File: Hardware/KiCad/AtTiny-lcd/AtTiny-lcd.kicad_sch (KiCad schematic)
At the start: 7 parts, among them J1 Conn_01x04_Pin, J2 Conn_01x04_Pin, Q1 BC817, U1 ATtiny414-SS

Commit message: cleanup #1
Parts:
- added C1: 100n, symbol Device:C
- R1: value R -> 1k
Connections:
- net +5V: now also C1.1
- net GND: now also C1.2
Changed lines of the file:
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@@
+	)
+	(junction
+		(at 81.28 116.84)
+		(diameter 0)
+		(color 0 0 0 0)
 	)
 	(junction
@@
 	)
 	(junction
+		(at 81.28 127)
+		(diameter 0)
+		(color 0 0 0 0)
+	)
+	(junction
 		(at 72.39 109.22)
 		(diameter 0)
@@
 	(wire
 		(pts
+			(xy 81.28 116.84) (xy 81.28 118.11)
+		)
+		(stroke
+			(width 0)
+			(type default)
+		)
+	)
+	(wire
+		(pts
 			(xy 88.9 121.92) (xy 88.9 95.25)
 		)
@@
 	(wire
 		(pts
+			(xy 81.28 125.73) (xy 81.28 127)
+		)
+		(stroke
+			(width 0)
+			(type default)
+		)
+	)
+	(wire
+		(pts
 			(xy 107.95 115.57) (xy 107.95 127)
 		)
@@
 	(wire
 		(pts
-			(xy 104.14 127) (xy 72.39 127)
+			(xy 104.14 127) (xy 81.28 127)
 		)
 		(stroke
@@
 		(pts
 			(xy 196.85 81.28) (xy 187.96 81.28)
+		)
+		(stroke
+			(width 0)
+			(type default)
+		)
+	)
+	(wire
+		(pts
+			(xy 81.28 127) (xy 72.39 127)
 		)
 		(stroke
@@
 			)
 		)
-		(property "Value" "R"
+		(property "Value" "1k"
 			(at 184.15 118.11 90)
 			(effects
@@
 					(unit 1)
 				)
+			)
+		)
+	)
+	(symbol
+		(lib_id "Device:C")
+		(at 81.28 121.92 0)
+		(unit 1)
+		(exclude_from_sim no)
+		(in_bom yes)
+		(on_board yes)
+		(dnp no)
+		(fields_autoplaced yes)
+		(property "Reference" "C1"
+			(at 85.09 120.6499 0)
+			(effects
+				(font
+					(size 1.27 1.27)
+				)
+				(justify left)
+			)
+		)
+		(property "Value" "100n"
+			(at 85.09 123.1899 0)
+			(effects
+				(font
+					(size 1.27 1.27)
+				)
+				(justify left)
+			)
+		)
+		(property "Footprint" ""
+			(at 82.2452 125.73 0)
+			(effects
+				(font
+					(size 1.27 1.27)
+				)
+				(hide yes)
+			)
+		)
+		(property "Datasheet" "~"
+			(at 81.28 121.92 0)
+			(effects
+				(font
+					(size 1.27 1.27)
+				)
+				(hide yes)
+			)
+		)
+		(property "Description" "Unpolarized capacitor"
+			(at 81.28 121.92 0)
+			(effects
+				(font
+					(size 1.27 1.27)
+				)
+				(hide yes)
+			)
+		)
+		(pin "2"
+		)
+		(pin "1"
+		)
+		(instances
+			(project "AtTiny-lcd"
+				(path "/788c3613-b442-483a-8dfb-af18bcc54a06"
+					(reference "C1")
+					(unit 1)
+				)

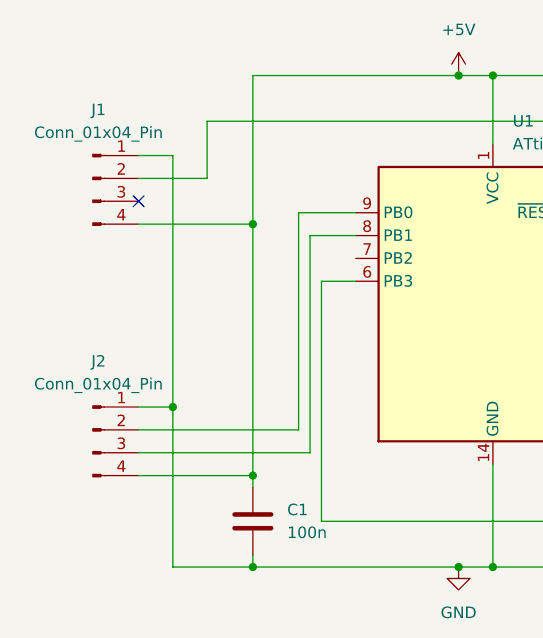
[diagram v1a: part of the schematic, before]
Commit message: Backlight dimming
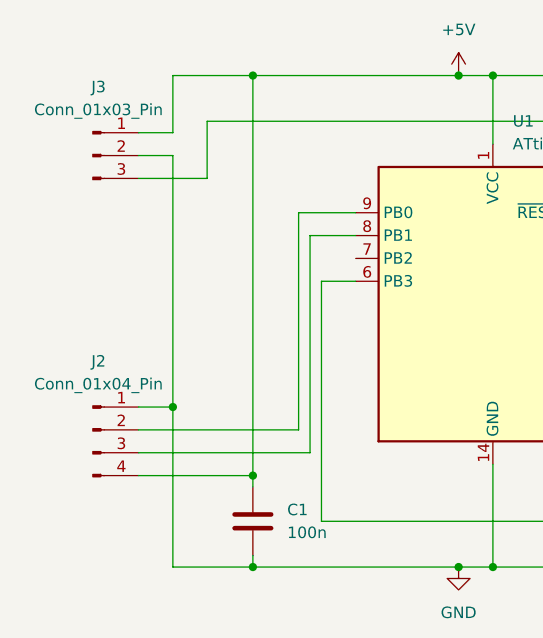
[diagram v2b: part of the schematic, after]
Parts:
- removed J1: Conn_01x04_Pin, Connector_PinHeader_2.54mm:PinHeader_1x04_P2.54mm_Vertical, symbol Connector:Conn_01x04_Pin
- added J3: Conn_01x03_Pin, Connector_PinHeader_2.54mm:PinHeader_1x03_P2.54mm_Vertical, symbol Connector:Conn_01x03_Pin
- C1: footprint (none) -> Capacitor_SMD:C_0805_2012Metric_Pad1.18x1.45mm_HandSolder
- R1: footprint Resistor_SMD:R_1210_3225Metric_Pad1.30x2.65mm_HandSolder -> Resistor_SMD:R_0805_2012Metric_Pad1.20x1.40mm_HandSolder
- RV1: footprint Potentiometer_SMD:Potentiometer_Bourns_TC33X_Vertical -> Potentiometer_SMD:Potentiometer_Vishay_TS53YJ_Vertical
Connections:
- net +5V: now also J3.1 (Pin_1)
- net GND: now also J3.2 (Pin_2)
- net at U1.10 (~{RESET}/PA0): now also J3.3 (Pin_3)
- no-connect marks 1 -> 0
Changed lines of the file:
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@@
-	)
-	(junction
-		(at 81.28 88.9)
-		(diameter 0)
-		(color 0 0 0 0)
 	)
 	(junction
@@
 	)
 	(junction
+		(at 81.28 72.39)
+		(diameter 0)
+		(color 0 0 0 0)
+	)
+	(junction
 		(at 196.85 127)
 		(diameter 0)
@@
 		(color 0 0 0 0)
 	)
-	(no_connect
-		(at 68.58 86.36)
-	)
 	(wire
 		(pts
@@
 	(wire
 		(pts
+			(xy 72.39 78.74) (xy 72.39 72.39)
+		)
+		(stroke
+			(width 0)
+			(type default)
+		)
+	)
+	(wire
+		(pts
+			(xy 68.58 81.28) (xy 72.39 81.28)
+		)
+		(stroke
+			(width 0)
+			(type default)
+		)
+	)
+	(wire
+		(pts
 			(xy 92.71 90.17) (xy 87.63 90.17)
 		)
@@
 	(wire
 		(pts
-			(xy 72.39 81.28) (xy 68.58 81.28)
-		)
-		(stroke
-			(width 0)
-			(type default)
-		)
-	)
-	(wire
-		(pts
 			(xy 123.19 97.79) (xy 134.62 97.79)
 		)
@@
 	(wire
 		(pts
+			(xy 68.58 78.74) (xy 72.39 78.74)
+		)
+		(stroke
+			(width 0)
+			(type default)
+		)
+	)
+	(wire
+		(pts
 			(xy 196.85 127) (xy 140.97 127)
 		)
@@
 	(wire
 		(pts
+			(xy 72.39 72.39) (xy 81.28 72.39)
+		)
+		(stroke
+			(width 0)
+			(type default)
+		)
+	)
+	(wire
+		(pts
 			(xy 76.2 83.82) (xy 76.2 77.47)
 		)
@@
 	(wire
 		(pts
-			(xy 81.28 88.9) (xy 81.28 116.84)
-		)
-		(stroke
-			(width 0)
-			(type default)
-		)
-	)
-	(wire
-		(pts
 			(xy 189.23 121.92) (xy 187.96 121.92)
 		)
@@
 	(wire
 		(pts
-			(xy 81.28 88.9) (xy 81.28 72.39)
+			(xy 81.28 72.39) (xy 81.28 116.84)
 		)
 		(stroke
@@
 		(pts
 			(xy 162.56 74.93) (xy 162.56 83.82)
-		)
-		(stroke
-			(width 0)
-			(type default)
-		)
-	)
-	(wire
-		(pts
-			(xy 68.58 88.9) (xy 81.28 88.9)
 		)
 		(stroke
@@
 			)
 		)
-		(property "Footprint" "Potentiometer_SMD:Potentiometer_Bourns_TC33X_Vertical"
+		(property "Footprint" "Potentiometer_SMD:Potentiometer_Vishay_TS53YJ_Vertical"
 			(at 214.63 88.9 0)
 			(effects
@@
 			)
 		)
-		(property "Footprint" "Resistor_SMD:R_1210_3225Metric_Pad1.30x2.65mm_HandSolder"
+		(property "Footprint" "Resistor_SMD:R_0805_2012Metric_Pad1.20x1.40mm_HandSolder"
 			(at 184.15 123.698 90)
 			(effects
@@
 				(path "/788c3613-b442-483a-8dfb-af18bcc54a06"
 					(reference "R1")
-					(unit 1)
-				)
-			)
-		)
-	)
-	(symbol
-		(lib_id "Connector:Conn_01x04_Pin")
-		(at 63.5 83.82 0)
-		(unit 1)
-		(exclude_from_sim no)
-		(in_bom yes)
-		(on_board yes)
-		(dnp no)
-		(fields_autoplaced yes)
-		(property "Reference" "J1"
-			(at 64.135 76.2 0)
-			(effects
-				(font
-					(size 1.27 1.27)
-				)
-			)
-		)
-		(property "Value" "Conn_01x04_Pin"
-			(at 64.135 78.74 0)
-			(effects
-				(font
-					(size 1.27 1.27)
-				)
-			)
-		)
-		(property "Footprint" "Connector_PinHeader_2.54mm:PinHeader_1x04_P2.54mm_Vertical"
-			(at 63.5 83.82 0)
-			(effects
-				(font
-					(size 1.27 1.27)
-				)
-				(hide yes)
-			)
-		)
-		(property "Datasheet" "~"
-			(at 63.5 83.82 0)
-			(effects
-				(font
-					(size 1.27 1.27)
-				)
-				(hide yes)
-			)
-		)
-		(property "Description" "Generic connector, single row, 01x04, script generated"
-			(at 63.5 83.82 0)
-			(effects
-				(font
-					(size 1.27 1.27)
-				)
-				(hide yes)
-			)
-		)
-		(pin "1"
-		)
-		(pin "3"
-		)
-		(pin "4"
-		)
-		(pin "2"
-		)
-		(instances
-			(project "AtTiny-lcd"
-				(path "/788c3613-b442-483a-8dfb-af18bcc54a06"
-					(reference "J1")
 					(unit 1)
 				)
@@
 			)
 		)
-		(property "Footprint" ""
+		(property "Footprint" "Capacitor_SMD:C_0805_2012Metric_Pad1.18x1.45mm_HandSolder"
 			(at 82.2452 125.73 0)
 			(effects
@@
 					(unit 1)
 				)
+			)
+		)
+	)
+	(symbol
+		(lib_id "Connector:Conn_01x03_Pin")
+		(at 63.5 81.28 0)
+		(unit 1)
+		(exclude_from_sim no)
+		(in_bom yes)
+		(on_board yes)
+		(dnp no)
+		(fields_autoplaced yes)
+		(property "Reference" "J3"
+			(at 64.135 73.66 0)
+			(effects
+				(font
+					(size 1.27 1.27)
+				)
+			)
+		)
+		(property "Value" "Conn_01x03_Pin"
+			(at 64.135 76.2 0)
+			(effects
+				(font
+					(size 1.27 1.27)
+				)
+			)
+		)
+		(property "Footprint" "Connector_PinHeader_2.54mm:PinHeader_1x03_P2.54mm_Vertical"
+			(at 63.5 81.28 0)
+			(effects
+				(font
+					(size 1.27 1.27)
+				)
+				(hide yes)
+			)
+		)
+		(property "Datasheet" "~"
+			(at 63.5 81.28 0)
+			(effects
+				(font
+					(size 1.27 1.27)
+				)
+				(hide yes)
+			)
+		)
+		(property "Description" "Generic connector, single row, 01x03, script generated"
+			(at 63.5 81.28 0)
+			(effects
+				(font
+					(size 1.27 1.27)
+				)
+				(hide yes)
+			)
+		)
+		(pin "1"
+		)
+		(pin "3"
+		)
+		(pin "2"
+		)
+		(instances
+			(project "AtTiny-lcd"
+				(path "/788c3613-b442-483a-8dfb-af18bcc54a06"
+					(reference "J3")
+					(unit 1)
+				)

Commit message: PCB updated
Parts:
- RV1: footprint Potentiometer_SMD:Potentiometer_Vishay_TS53YJ_Vertical -> ownFootprints:Potentiometer_SMD_EBay_10k
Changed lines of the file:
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@@
 			)
 		)
-		(property "Footprint" "Potentiometer_SMD:Potentiometer_Vishay_TS53YJ_Vertical"
+		(property "Footprint" "ownFootprints:Potentiometer_SMD_EBay_10k"
 			(at 214.63 88.9 0)
 			(effects

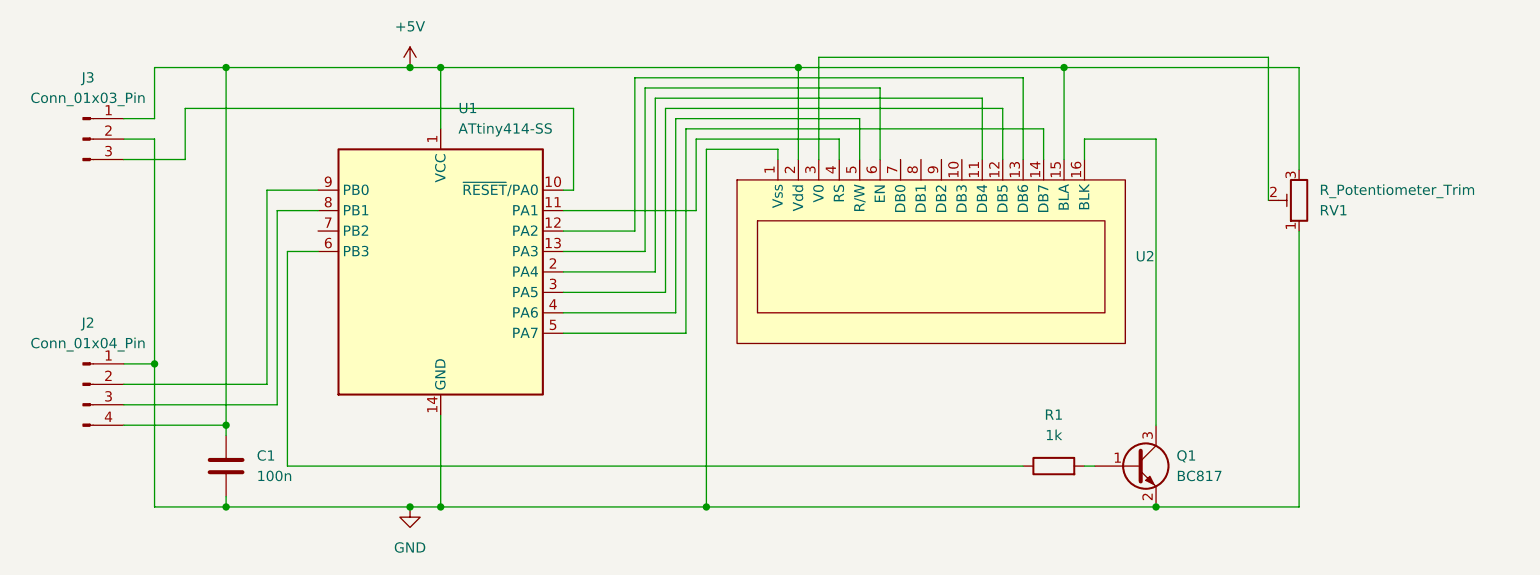
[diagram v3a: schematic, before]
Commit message: updated PCB dimming through ISR
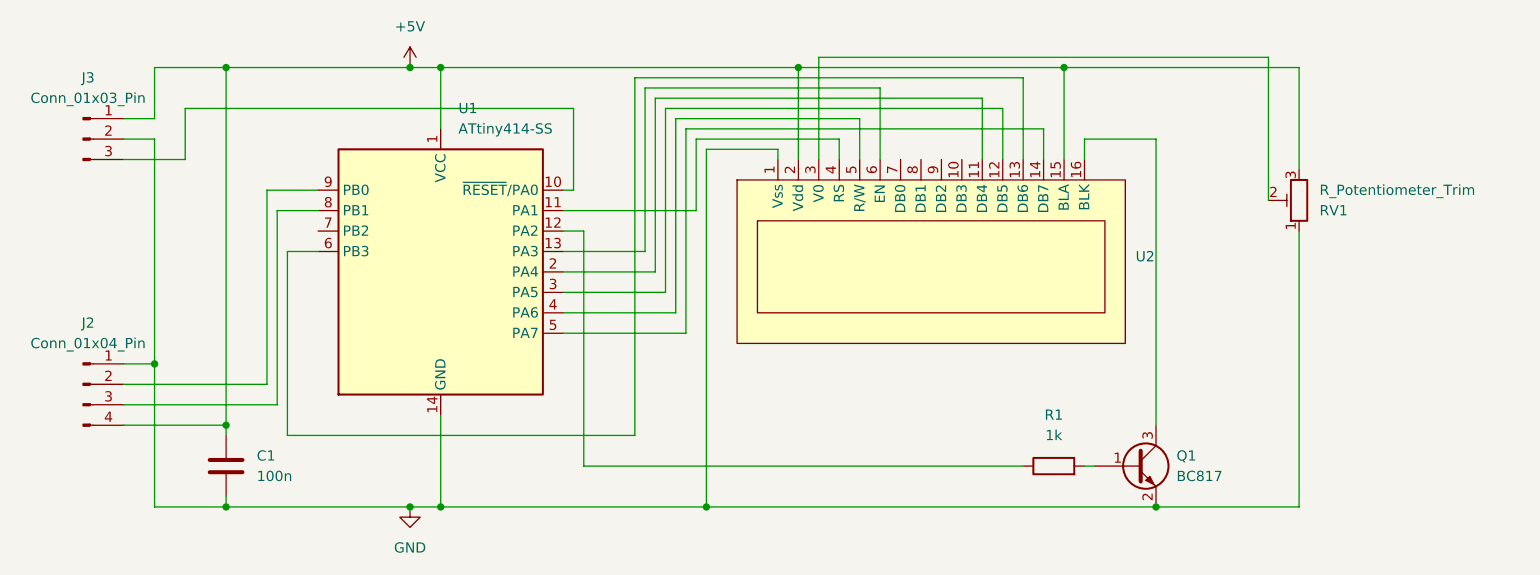
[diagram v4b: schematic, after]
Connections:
- net at U1.12 (PA2): now also R1.1; no longer U2.13 (DB6)
- net at U1.6 (PB3): now also U2.13 (DB6); no longer R1.1
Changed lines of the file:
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@@
+	(wire
+		(pts
+			(xy 88.9 118.11) (xy 88.9 95.25)
+		)
+		(stroke
+			(width 0)
+			(type default)
+		)
+	)
 	(wire
 		(pts
@@
 	(wire
 		(pts
+			(xy 180.34 121.92) (xy 125.73 121.92)
+		)
+		(stroke
+			(width 0)
+			(type default)
+		)
+	)
+	(wire
+		(pts
+			(xy 132.08 118.11) (xy 88.9 118.11)
+		)
+		(stroke
+			(width 0)
+			(type default)
+		)
+	)
+	(wire
+		(pts
 			(xy 123.19 97.79) (xy 134.62 97.79)
 		)
@@
 	(wire
 		(pts
-			(xy 88.9 121.92) (xy 88.9 95.25)
-		)
-		(stroke
-			(width 0)
-			(type default)
-		)
-	)
-	(wire
-		(pts
 			(xy 132.08 73.66) (xy 180.34 73.66)
 		)
@@
 	(wire
 		(pts
+			(xy 88.9 95.25) (xy 92.71 95.25)
+		)
+		(stroke
+			(width 0)
+			(type default)
+		)
+	)
+	(wire
+		(pts
 			(xy 87.63 114.3) (xy 68.58 114.3)
 		)
@@
 	(wire
 		(pts
+			(xy 125.73 121.92) (xy 125.73 92.71)
+		)
+		(stroke
+			(width 0)
+			(type default)
+		)
+	)
+	(wire
+		(pts
 			(xy 196.85 127) (xy 140.97 127)
 		)
@@
 	(wire
 		(pts
-			(xy 132.08 92.71) (xy 132.08 73.66)
-		)
-		(stroke
-			(width 0)
-			(type default)
-		)
-	)
-	(wire
-		(pts
-			(xy 180.34 121.92) (xy 88.9 121.92)
-		)
-		(stroke
-			(width 0)
-			(type default)
-		)
-	)
-	(wire
-		(pts
 			(xy 107.95 72.39) (xy 107.95 80.01)
 		)
@@
 	(wire
 		(pts
+			(xy 132.08 73.66) (xy 132.08 118.11)
+		)
+		(stroke
+			(width 0)
+			(type default)
+		)
+	)
+	(wire
+		(pts
 			(xy 81.28 72.39) (xy 81.28 116.84)
 		)
@@
 	(wire
 		(pts
-			(xy 123.19 92.71) (xy 132.08 92.71)
-		)
-		(stroke
-			(width 0)
-			(type default)
-		)
-	)
-	(wire
-		(pts
 			(xy 139.7 90.17) (xy 139.7 81.28)
 		)
@@
 	(wire
 		(pts
-			(xy 88.9 95.25) (xy 92.71 95.25)
-		)
-		(stroke
-			(width 0)
-			(type default)
-		)
-	)
-	(wire
-		(pts
 			(xy 86.36 87.63) (xy 92.71 87.63)
 		)
 		(stroke
+			(width 0)
+			(type default)
+		)
+	)
+	(wire
+		(pts
+			(xy 125.73 92.71) (xy 123.19 92.71)
+		)
+		(stroke

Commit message: update
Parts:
- U2: footprint ownFootprints:LCD2004 -> ownFootprints:LCD2008
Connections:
- net +5V: now also RV1.1; no longer RV1.3
- net GND: now also RV1.3; no longer RV1.1
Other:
- moved on the sheet: RV1
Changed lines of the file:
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@@
 	(symbol
 		(lib_id "Device:R_Potentiometer_Trim")
-		(at 214.63 88.9 180)
+		(at 214.63 88.9 0)
+		(mirror y)
 		(unit 1)
 		(exclude_from_sim no)
@@
 		(dnp no)
 		(property "Reference" "RV1"
-			(at 217.17 90.1701 0)
+			(at 217.17 87.6299 0)
 			(effects
 				(font
@@
 		)
 		(property "Value" "R_Potentiometer_Trim"
-			(at 217.17 87.6301 0)
+			(at 217.17 90.1699 0)
 			(effects
 				(font
@@
 			)
 		)
-		(property "Footprint" "ownFootprints:LCD2004"
+		(property "Footprint" "ownFootprints:LCD2008"
 			(at 147.32 85.09 0)
 			(effects
